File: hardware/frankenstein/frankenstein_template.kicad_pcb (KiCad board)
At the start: 2 copper layers, 0 parts

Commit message: 
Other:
- board outline added: 100 x 99.9 mm
- net class Default: clearance 0.254 -> 0.2032
- rule trace_clearance: 0.254 -> 0.2032
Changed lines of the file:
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@@
     (links 0)
     (no_connects 0)
-    (area 120.549999 93.244999 186.790001 190.600001)
+    (area 120.549999 92.024999 225.550001 192.074001)
     (thickness 1.6)
-    (drawings 12)
+    (drawings 16)
     (tracks 0)
     (zones 0)
@@
   (setup
     (last_trace_width 0.254)
-    (trace_clearance 0.254)
+    (trace_clearance 0.2032)
     (zone_clearance 0.508)
     (zone_45_only no)
@@
   (net 0 "")
   (net_class Default "This is the default net class."
-    (clearance 0.254)
+    (clearance 0.2032)
     (trace_width 0.254)
     (via_dia 0.889)
@@
     (add_net "")
   )
+  (gr_line (start 125.5 192.024) (end 125.5 92.075) (angle 90) (layer Edge.Cuts) (width 0.1))
+  (gr_line (start 225.5 192.024) (end 125.5 192.024) (angle 90) (layer Edge.Cuts) (width 0.1))
+  (gr_line (start 225.5 92.075) (end 225.5 192.024) (angle 90) (layer Edge.Cuts) (width 0.1))
+  (gr_line (start 125.5 92.075) (end 225.5 92.075) (angle 90) (layer Edge.Cuts) (width 0.1))
   (gr_line (start 120.65 93.345) (end 186.69 93.345) (angle 90) (layer Cmts.User) (width 0.2))
   (gr_line (start 186.69 190.5) (end 186.69 93.472) (angle 90) (layer Cmts.User) (width 0.2))

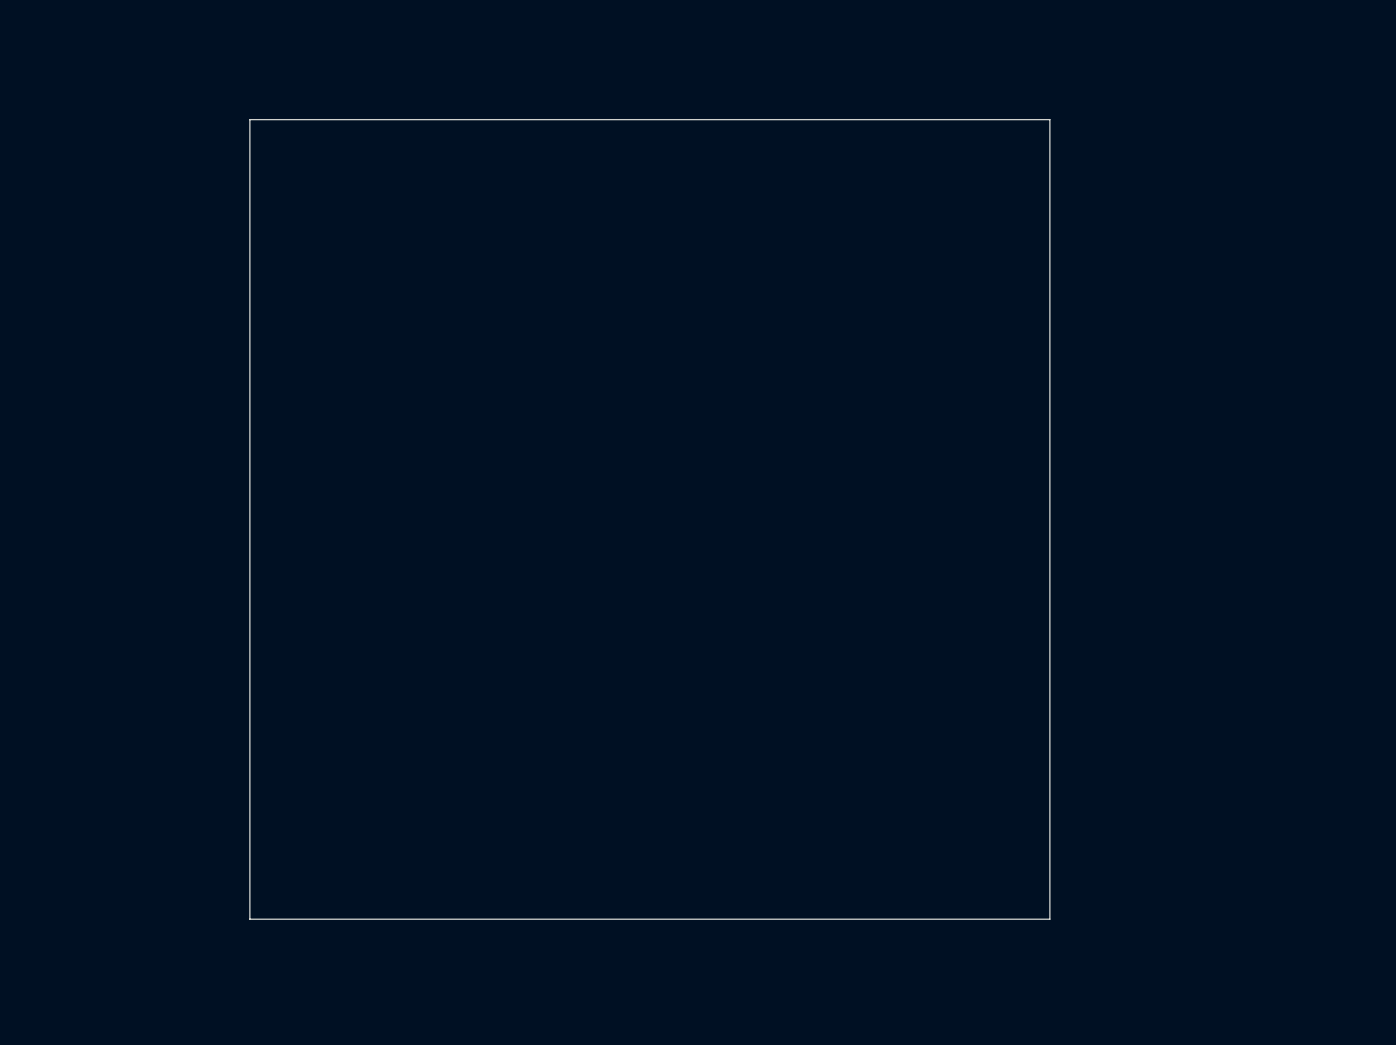
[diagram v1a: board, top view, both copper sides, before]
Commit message: 
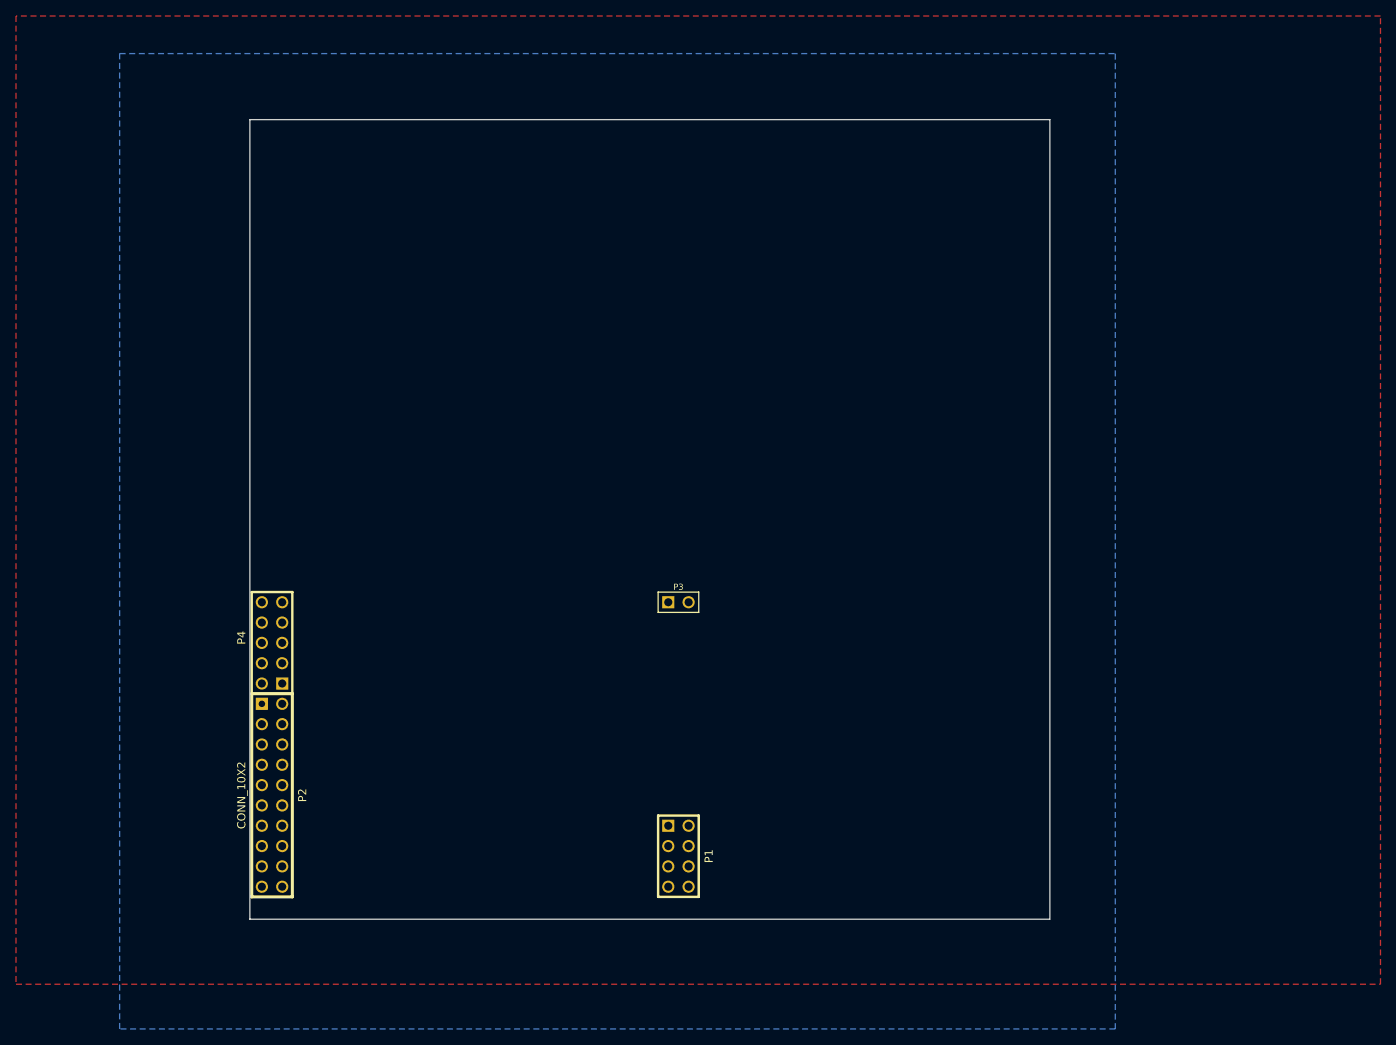
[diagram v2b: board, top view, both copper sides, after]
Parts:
- added P1: CONN_4X2, pin_array_4x2, F.Cu at (179.1, 184.2)
- added P2: CONN_10X2, PIN_ARRAY_10X2, F.Cu at (128.3, 176.5)
- added P3: CONN_2, PIN_ARRAY_2X1, F.Cu at (179.1, 152.4)
- added P4: CONN_5X2, PIN_ARRAY_5x2, F.Cu at (128.3, 157.5)
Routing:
- added copper zone on B.Cu, net GND
- added copper zone on F.Cu, net GND
